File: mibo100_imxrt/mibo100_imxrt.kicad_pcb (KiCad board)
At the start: 2 copper layers, 66 x 25.4 mm, 49 parts, among them J1 Conn_01x26, J2 Conn_01x26, J3 Conn_02x02_Odd_Even, J4 USB_B_Micro, J5 Conn_01x05, SW1 SW_Push, U1 MIMXRT1021CAF4A, U2 W25X80, U3 AP3417C, Y1 24MHz

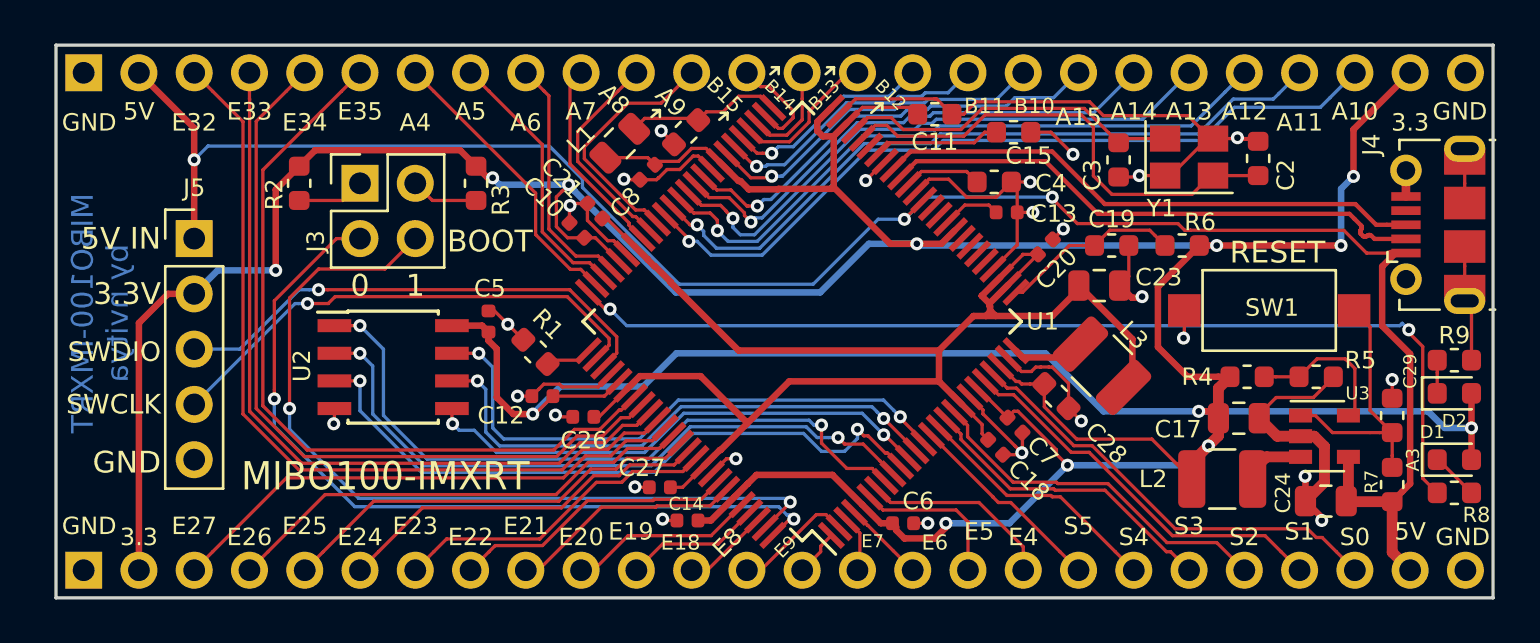
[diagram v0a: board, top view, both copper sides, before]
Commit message: POR_B and double capacitors
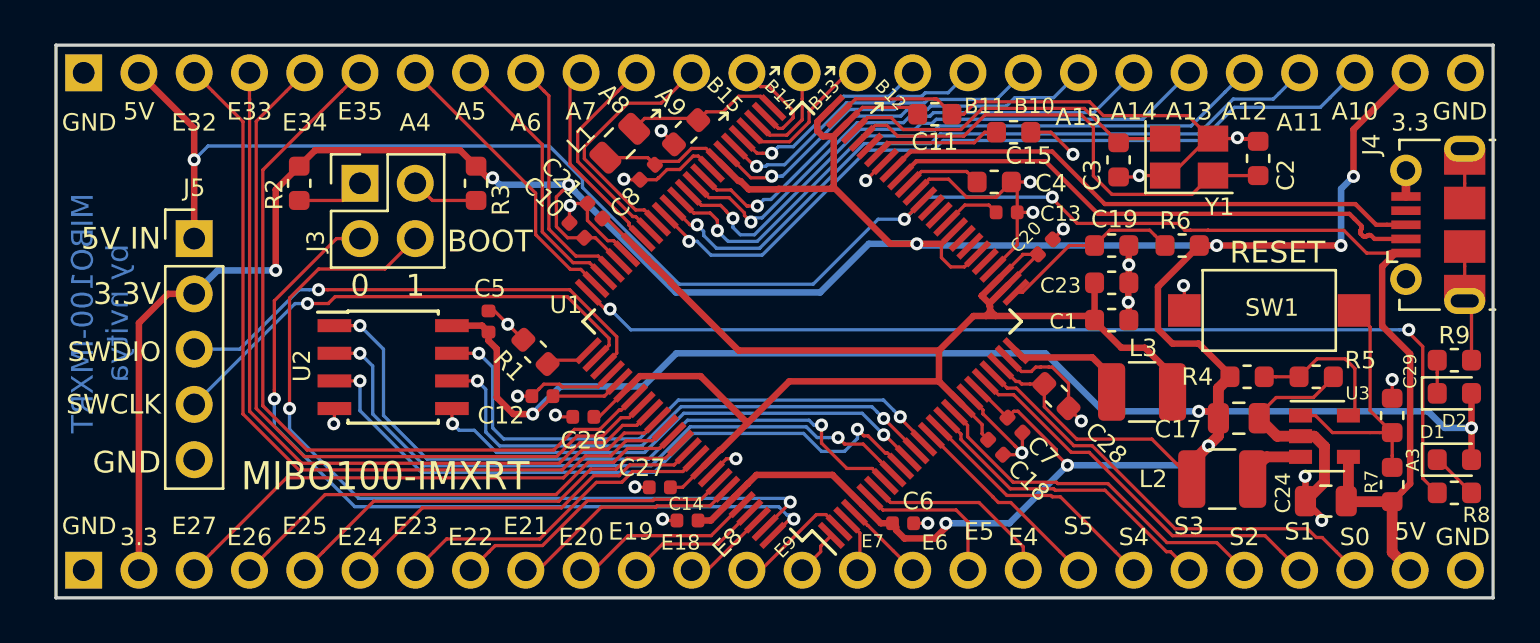
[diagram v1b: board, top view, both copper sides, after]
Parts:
- added C1: 22uF, Capacitor_SMD:C_0603_1608Metric, F.Cu at (159.0, 82.5)
- C23: value 33uF -> 22uF; footprint Capacitor_SMD:C_0805_2012Metric -> Capacitor_SMD:C_0603_1608Metric
- moved L3 2.20 mm to (160.4, 85.8), turned to 0 degrees
- moved C23 0.59 mm to (159.0, 80.8)
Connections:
- U1 pad 31: Net-(U1-Pad31) -> +3V3
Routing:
- net +3V3: track 240.9 -> 243.2 mm
- net Net-(L3-Pad1): track 3.34 -> 5.59 mm
- net /DCDC_OUT: track 67.9 -> 69.3 mm
- net GND: vias 25 -> 26
